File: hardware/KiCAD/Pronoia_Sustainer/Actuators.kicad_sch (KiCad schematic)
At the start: 40 parts, among them J10 Screw_Terminal_01x02, J11 Screw_Terminal_01x02, J3 Screw_Terminal_01x02, J4 Servo0, J5 Servo0, J6 Servo0, J7 Servo0, J8 Screw_Terminal_01x02, J9 Screw_Terminal_01x02, Q1 AO3400A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

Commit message: Completed 1st draft of Schematic
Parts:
- removed D5: SS14, PCM_JLCPCB:D_SMA, symbol PCM_JLCPCB-Diodes:Schottky,SS14
- removed J11: Screw_Terminal_01x02, TerminalBlock_Phoenix:TerminalBlock_Phoenix_MKDS-1,5-2-5.08_1x02_P5.08mm_Horizontal, symbol Connector:Screw_Terminal_01x02
- removed Q5: AO3400A, PCM_JLCPCB:Q_SOT-23, symbol PCM_JLCPCB-Transistors:NMOS,AO3400A
- removed R19: 100Ω, PCM_JLCPCB:R_0805, symbol PCM_JLCPCB-Resistors:0805,100Ω
- removed R20, R22: 10kΩ, PCM_JLCPCB:R_0805, symbol PCM_JLCPCB-Resistors:0805,10kΩ
- removed R21: 18kΩ, PCM_JLCPCB:R_0805, symbol PCM_JLCPCB-Resistors:0805,18kΩ
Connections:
- net ServoPWM2: now also J6.3 (Pin_3)
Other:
- note added: "Pyro Channels (4 total) 1 for Sustainer Stage Motor 2 for parachutee deployment 1 Extra"
- note added: "Servo Motor Connections (4 total)"
- moved on the sheet: D1, D2, D3, D4, J10, J3, J8, J9, Q1, Q2, Q3, Q4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

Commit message: Last commit for KiCAD schematic w/ GPS, Telem, and Bluetooth
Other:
- note added: "4 E-matches (Order and Connect via Screw Terminal Block)"
- note removed: "5 E-matches (Order and Connect via Screw Terminal Block)"
- company: (none) -> Walla Walla University
- title: (none) -> Pronoia Sustainer Actuators
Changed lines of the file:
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@@
 	(generator_version "9.0")
 	(paper "A4")
-	(text "5 E-matches (Order and Connect via Screw Terminal Block)"
+	(title_block
+		(title "Pronoia Sustainer Actuators")
+		(date "2026-02-03")
+		(rev "1.0")
+		(company "Walla Walla University")
+		(comment 1 "Prometheus Rocket Project")
+	)
+	(text "4 E-matches (Order and Connect via Screw Terminal Block)"
 		(exclude_from_sim no)
 		(at 253.238 23.368 0)

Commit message: Finalized v2.0 of Pronoia Schematic
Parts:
- removed J10, J3, J8, J9: Screw_Terminal_01x02, TerminalBlock_Phoenix:TerminalBlock_Phoenix_MKDS-1,5-2-5.08_1x02_P5.08mm_Horizontal, symbol Connector:Screw_Terminal_01x02
- added C15, C16, C17, C7: 100nF, PCM_JLCPCB:C_0402, symbol PCM_JLCPCB-Capacitors:0402,100nF
- added C18: 1000 uF, EEE-FT1A102AP, Capacitor_SMD:CP_Elec_8x10.5, symbol Device:C_Polarized
- added J3: 1751303, 1751303:1751303, symbol 1751303:1751303
- C6: value 470 uF -> 1000 uF, EEE-FT1A102AP; footprint Capacitor_SMD:CP_Elec_8x10 -> Capacitor_SMD:CP_Elec_8x10.5; LCSC C970706 -> C278408
- J4, J5, J6, J7: now not fitted
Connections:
- net PyroChannelPower: now also C18.1, J3.1, J3.3, J3.5, J3.7
- net Pyro1-: now reaches D2.2, Q2.3 (D), R9.1
- net Pyro1-: now also C15.1, J3.4
- net Pyro2-: now reaches D3.2, Q3.3 (D), R13.1
- net Pyro2-: now also C16.1, J3.6
- net Pyro3-: now reaches D4.2, Q4.3 (D), R17.1
- net Pyro3-: now also C17.1, J3.8
- net Pyro0-: now reaches D1.2, Q1.3 (D), R5.1
- net Pyro0-: now also C7.1, J3.2
- net GNDPWR renamed GND
- net GND: now also C15.2, C16.2, C17.2, C18.2, C7.2
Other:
- note added: "1x8 Pyro Channel Screw Terminal Block"
- note added: "Pyro Channels (4 total) 1 for Sustainer Stage Motor 1 for parachute deployment 1 for Stage Separation 1 Extra for the drogue chute w/ timed ejection charge backup"
- note removed: "Pyro Channels (4 total) 1 for Sustainer Stage Motor 2 for parachutee deployment 1 Extra"
- moved on the sheet: D1, D2, D3, D4, Q1, Q2, Q3, Q4, R10, R11, R12, R13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

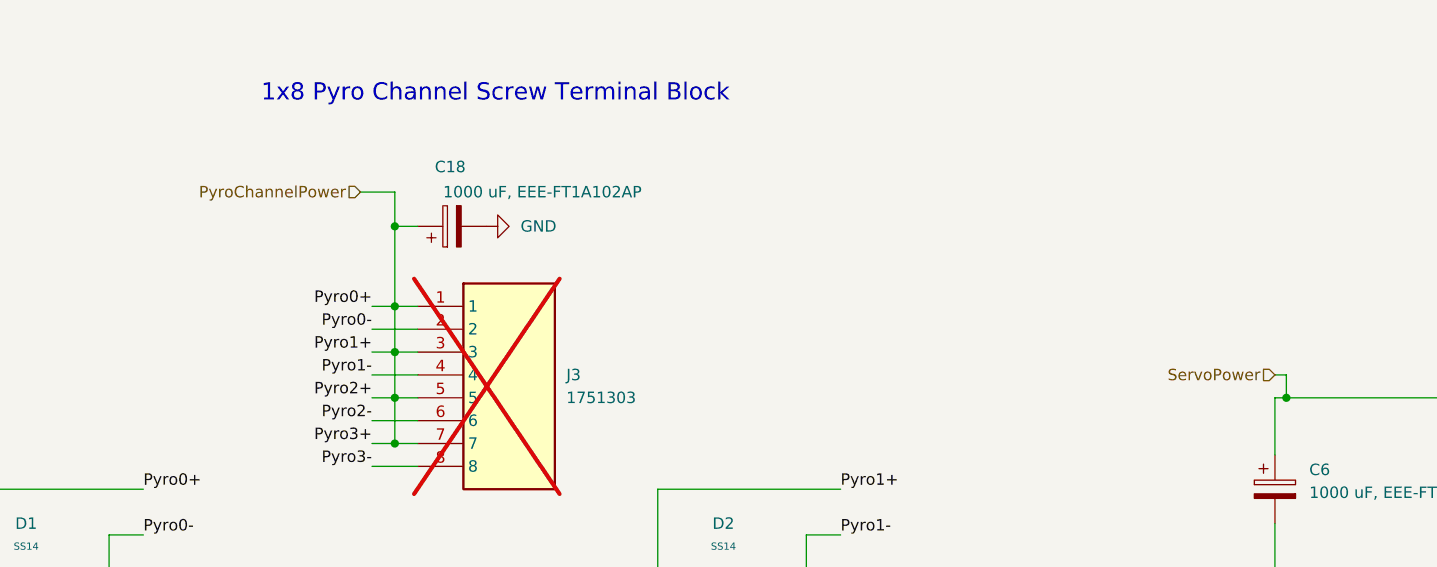
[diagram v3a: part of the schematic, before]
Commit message: Finished PCB layout
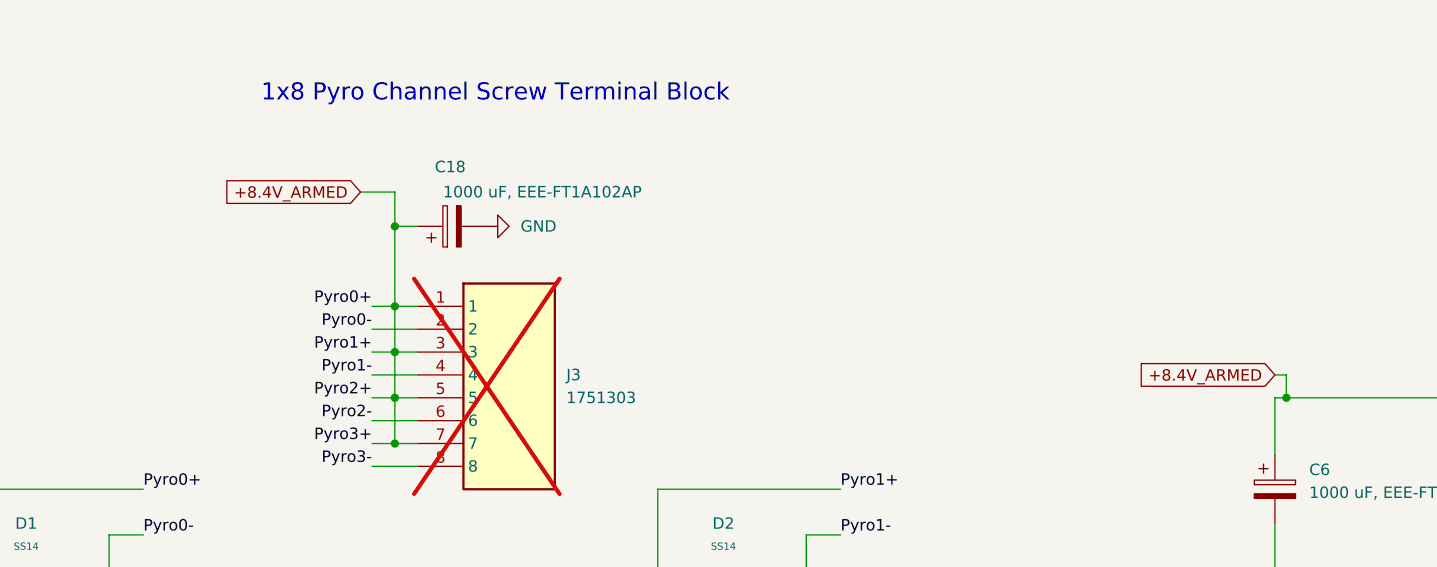
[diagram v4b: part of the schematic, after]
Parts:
- removed R13, R17, R5, R9: 18kΩ, PCM_JLCPCB:R_0805, symbol PCM_JLCPCB-Resistors:0805,18kΩ
- added R13, R17, R5, R9: 18kΩ, PCM_JLCPCB:R_0603, symbol PCM_JLCPCB-Resistors:0603,18kΩ
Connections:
- net ServoPower is gone; now on net +8.4V_ARMED: C6.1, J4.2 (Pin_2), J5.2 (Pin_2), J6.2 (Pin_2), J7.2 (Pin_2)
- net Pyro0-: now also R5.1
- net Pyro1-: now also R9.1
- net Pyro2-: now also R13.1
- net Pyro3-: now also R17.1
- net PyroSense0: now also R5.2
- net PyroSense1: now also R9.2
- net PyroSense2: now also R13.2
- net PyroSense3: now also R17.2
- net PyroChannelPower renamed +8.4V_ARMED

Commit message: Sensor Bring-Up
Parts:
- J3, J4, J5, J6, J7: now left out of the parts list
